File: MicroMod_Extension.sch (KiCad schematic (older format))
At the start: 1 part, among them J1 2199230-4

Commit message: inductor type
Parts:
- added C1, C2, C3, C5: 100n, Capacitor_SMD:C_0402_1005Metric, symbol Device:C
- added C4: 47n, Capacitor_SMD:C_0402_1005Metric, symbol Device:C
- added C?: 1u, Capacitor_SMD:C_0402_1005Metric, symbol Device:C
- added C?: 220p, Capacitor_SMD:C_0402_1005Metric, symbol Device:C
- added J2: XKB_U262-16XN-4BVC11, Connector_USB:USB_C_Receptacle_XKB_U262-16XN-4BVC11, symbol MicroMod_Extension:XKB_U262-16XN-4BVC11
- added L?: 2nH, symbol Device:L
- added U1: 24aa64ft-eot, Package_TO_SOT_SMD:SOT-23-5, symbol MicroMod_Extension:24aa64ft-eot
- added U2: nRF51822-QFAA-R7, Package_DFN_QFN:QFN-48-1EP_6x6mm_P0.4mm_EP4.6x4.6mm, symbol MCU_Nordic:nRF51x22-QFxx
- added U?: RFX2411N, symbol MicroMod_Extension:RFX2411N
- added Y1: TSX-3225_16.0000MF18X-AC3, XTAL_TSX-3225_16.0000MF18X-AC3, symbol MicroMod_Extension:TSX-3225_16.0000MF18X-AC3
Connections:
- net E_SCL: now also U1.1 (SCL)
- net E_SDA: now also U1.3 (SDA)
- net GND: now also C2.2, C3.2, C4.1, C5.1, C?.2, C?.2, J2.A1 (GND), J2.A12 (GND), J2.B1 (GND), J2.B12 (GND), J2.S1 (SHELD), U1.2 (VSS), U1.5 (WP), U2.13 (VSS), U2.33 (VSS), U2.34 (VSS), U2.49 (EP), U?.1 (GND), U?.11 (GND), U?.13 (GND), U?.19 (GND), U?.21 (GND), Y1.2 (GND), Y1.4 (GND)
- net OTG_FS_D+: now also J2.A7 (D-), J2.B7 (D-)
- net OTG_FS_D-: now also J2.A6 (D+), J2.B6 (D+)
- net VBAT: now also U2.1 (VDD), U2.12 (VDD), U2.35 (AVDD), U2.36 (AVDD)
- net VCC: now also U1.4 (VCC)
- new net: C4.2, U2.29 (DEC2)
- new net: C2.1, U2.37 (XC1), Y1.1
- new net: C3.1, U2.38 (XC2), Y1.3 (2)
- new net: C5.2, U2.39 (DEC1)
- new net: C?.1, C?.1, U?.18 (VDD), U?.20 (VDD)
- new net NRF_SWCLK: U2.24 (SWDCLK)
- new net NRF_SWIO: U2.23 (SWDIO/~RST)
- new net VBUS: J2.A4 (VBUS), J2.A9 (VBUS), J2.B4 (VBUS), J2.B9 (VBUS)
- no-connect marks 0 -> 19

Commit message: update RF
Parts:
- removed C?: 1u, Capacitor_SMD:C_0402_1005Metric, symbol Device:C
- removed C?: 220p, Capacitor_SMD:C_0402_1005Metric, symbol Device:C
- removed L?: 2nH, symbol Device:L
- removed U?: RFX2411N, symbol MicroMod_Extension:RFX2411N
- added C? (x2): 220p, Capacitor_SMD:C_0402_1005Metric, symbol Device:C
- added C?: 4.7u, Capacitor_SMD:C_0402_1005Metric, symbol Device:C
- added C?: 2.2n, Capacitor_SMD:C_0402_1005Metric, symbol Device:C
- added C?: 2.5p, Capacitor_SMD:C_0402_1005Metric, symbol Device:C
- added E?: 2450AT18B100E, MicroMod_Extension:XDCR_2450AT18B100E, symbol MicroMod_Extension:2450AT18B100E
- added FL1: 2450BM14E0003T, FIL_2450BM14E0003T, symbol MicroMod_Extension:2450BM14E0003T
- added FL? (x2): ADFC15-2450.00-A-T, MicroMod_Extension:FIL_ADFC15-2450.00-A-T, symbol MicroMod_Extension:ADFC15-2450.00-A-T
- added J?: RSP-122811-01, MicroMod_Extension:SAMTEC_RSP-122811-01, symbol MicroMod_Extension:RSP-122811-01
- added L? (x2): 2nH, Inductor_SMD:L_0402_1005Metric, symbol Device:L
- added L?: 1nH, Inductor_SMD:L_0402_1005Metric, symbol Device:L
- added L?: 4.7nH, Inductor_SMD:L_0402_1005Metric, symbol Device:L
- added R? (x2): 10K, Resistor_SMD:R_0402_1005Metric, symbol Device:R
- added U?: RFX2411N, symbol MicroMod_Extension:RFX2411N
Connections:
- net GND: now also C?.1, C?.1, C?.1, C?.1, FL1.2 (GND), FL1.6 (GND), FL?.1 (GND), FL?.1 (GND), FL?.3 (GND), FL?.3 (GND), J?.G1, J?.G2, L?.2, L?.2, U?.1 (GND), U?.11 (GND), U?.13 (GND), U?.19 (GND), U?.2 (NC), U?.21 (GND), U?.4 (NC)
- net at U2.30 (VDD_PA): now also C?.2, FL1.5 (DC_FEED), R?.1
- net at U2.31 (ANT1): now also FL1.3 (BALANCED_PORT1)
- net at U2.32 (ANT2): now also FL1.4 (BALANCED_PORT2)
- new net: FL1.1 (UNBALANCED_PORT), U?.5 (TXRX)
- new net: FL?.2 (OUT/IN), J?.1
- new net: FL?.4 (IN/OUT), U?.12 (ANT_B)
- new net: FL?.4 (IN/OUT), U?.14 (ANT_A)
- new net: L?.1, U?.15 (IND)
- new net: C?.2, C?.2, C?.2, U?.18 (VDD), U?.20 (VDD)
- new net: R?.2, U?.6 (TXEN)
- new net: C?.2, FL?.2 (OUT/IN)
- new net: C?.1, L?.1, L?.2
- new net: E?.1, L?.1
- new net PA_MODE: U?.9 (MODE)
- new net PA_RXEN: U?.7 (RXEN)
- new net PA_SW_ANT: U?.10 (SW_ANT)
- no-connect marks 19 -> 18
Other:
- note added: "4-layer, single ended, JLC7628: 11.55mil track width on outer layer"
- note added: "This balun matches ANT1 and ANT2 to 50 ohm."
- note added: "this line should have 50ohm inpedence matching"
- moved on the sheet: C2, C3, C4, C5, U2, Y1

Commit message: add power management
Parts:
- added C10, C19, C20, C21, C22: 1u, Capacitor_SMD:C_0402_1005Metric, symbol Device:C
- added C12: 10u, Capacitor_SMD:C_0402_1005Metric, symbol Device:C
- added C13, C9: 10n, Capacitor_SMD:C_0402_1005Metric, symbol Device:C
- added C18: 22u, Capacitor_SMD:C_0402_1005Metric, symbol Device:C
- added C6, C7, C8: 100n, Capacitor_SMD:C_0402_1005Metric, symbol Device:C
- added D1: LED, MicroMod_Extension:LED-0603, symbol Device:LED
- added D2, D4: 150066RG74000, MicroMod_Extension:150066RG74000, symbol MicroMod_Extension:150066RG74000
- added D3: SMF4L17A, Diode_SMD:D_SOD-123, symbol Device:D_TVS
- added D5: MBR0520-TP, Diode_SMD:D_SOD-123, symbol Device:D
- added L5: 2.2uH-TYA2520102R2M-10, Inductor_SMD:L_1008_2520Metric, symbol Device:L
- added R1, R10, R5, R8, R9: 150r, Resistor_SMD:R_0402_1005Metric, symbol Device:R
- added R11: 510k, Resistor_SMD:R_0402_1005Metric, symbol Device:R
- added R12: 110k, Resistor_SMD:R_0402_1005Metric, symbol Device:R
- added R14: 430K, Resistor_SMD:R_0402_1005Metric, symbol Device:R
- added R15: 82K, Resistor_SMD:R_0402_1005Metric, symbol Device:R
- added R2, R3: 5.1k, Resistor_SMD:R_0402_1005Metric, symbol Device:R
- added R6, R7: 10K, Resistor_SMD:R_0402_1005Metric, symbol Device:R
- added SW1: TL1014BF160QG, MicroMod_Extension:E-Switch-TL1014BF160QG-0, symbol MicroMod_Extension:TL1014BF160QG
- added TP1, TP2, TP3: TestPoint, TestPoint:TestPoint_Pad_D1.0mm, symbol Connector:TestPoint
- added U4: TPS62170DSG, Package_SON:WSON-8-1EP_2x2mm_P0.5mm_EP0.9x1.6mm_ThermalVias, symbol Regulator_Switching:TPS62170DSG
- added U5, U6: NCP702SN30T1G, Package_TO_SOT_SMD:TSOT-23-5, symbol MicroMod_Extension:NCP702SN30T1G
- C2, C3: value 100n -> 12p
- U3: renamed from U?; footprint (none) -> Package_DFN_QFN:QFN-20-1EP_3x3mm_P0.4mm_EP1.65x1.65mm
- gave numbers to parts that had none: 15
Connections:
- net BOOT0 is gone; now on net STM_BOOT0: J1.70
- net NRST is gone; now on net STM_NRST: J1.67
- net OTG_FS_VBUS is gone; now on net VBUS: J1.9
- net GND: now also C10.2, C12.2, C13.2, C18.1, C19.1, C20.1, C21.2, C22.2, C6.2, C7.2, C8.2, C9.2, D1.1 (K), D3.2 (A2), R12.2, R15.1, R2.2, R3.2, R7.2, SW1.2, SW1.4, U4.1 (PGND), U4.4 (AGND), U4.9 (PAD), U5.2 (GND), U6.2 (GND)
- net GREEN_L: now also R8.1
- net GREEN_R: now also R10.1
- net NRF_CTRL: now also U2.20 (P0.14)
- net NRF_RX: now also U2.3 (P0.30)
- net NRF_TX: now also U2.48 (P0.29)
- net PA_MODE: now also U2.27 (P0.19)
- net PA_RXEN: now also U2.28 (P0.20)
- net PA_SW_ANT: now also U2.26 (P0.18)
- net RED_L: now also R5.1
- net RED_R: now also R9.1
- net VBAT: now also U2.5 (P0.1), C13.1, R11.2, R12.1; no longer J1.73, U2.1 (VDD), U2.12 (VDD), U2.35 (AVDD), U2.36 (AVDD)
- net VBUS: now also D5.2 (A), R6.1
- net VCC: now also C21.1, D2.3, D2.4, D4.3, D4.4, TP2.1, U6.5 (OUT)
- net VEN_D: now reaches U2.16 (P0.10)
- net VEN_D: now also R6.2, R7.1, U6.3 (EN)
- net LED_BLUE: now reaches U2.19 (P0.13)
- net LED_BLUE: now also R1.1
- net SWITCH: now reaches U2.25 (P0.17)
- net SWITCH: now also SW1.1, SW1.3
- net STM_NRST: now reaches U2.40 (P0.21)
- net STM_BOOT0: now reaches U2.41 (P0.22)
- net PM_PGOOD: now reaches U2.8 (P0.4)
- net PM_PGOOD: now also U4.8 (PG)
- net VCC_NRF: now reaches C14.2, C15.2, C16.2, U3.18 (VDD), U3.20 (VDD)
- net VCC_NRF: now also J1.73, U2.1 (VDD), U2.12 (VDD), U2.35 (AVDD), U2.36 (AVDD), C10.1, C22.1, C6.1, C7.1, C8.1, C9.1, TP3.1, U5.5 (OUT)
- net at J2.A5 (CC1): now also R2.1
- net at J2.B5 (CC2): now also R3.1
- net E_SPI_CLK renamed E_SPI_SCK
- net SPI2_CLK renamed SPI2_SCK
- new net: R14.1, R15.2, U4.5 (FB)
- new net: C18.2, C19.2, C20.2, D5.1 (K), L5.1, R14.2, TP1.1, U4.6 (VOS), U5.1 (IN), U5.3 (EN), U6.1 (IN)
- new net: L5.2, U4.7 (SW)
- new net: D1.2 (A), R1.2
- new net: D2.1, R5.2
- new net: D2.2, R8.2
- new net: D4.1, R9.2
- new net: D4.2, R10.2
- new net BATT: C12.1, D3.1 (A1), R11.1, U4.2 (VIN), U4.3 (EN)
- no-connect marks 18 -> 33
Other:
- note added: "4-layer, single ended, JLC7628: 11.55mil track width on outer layer for 50 ohm."
- note added: "EEPROM"
- note added: "USB-C"
- note removed: "4-layer, single ended, JLC7628: 11.55mil track width on outer layer"
- note removed: "this line should have 50ohm inpedence matching"
- moved on the sheet: U1

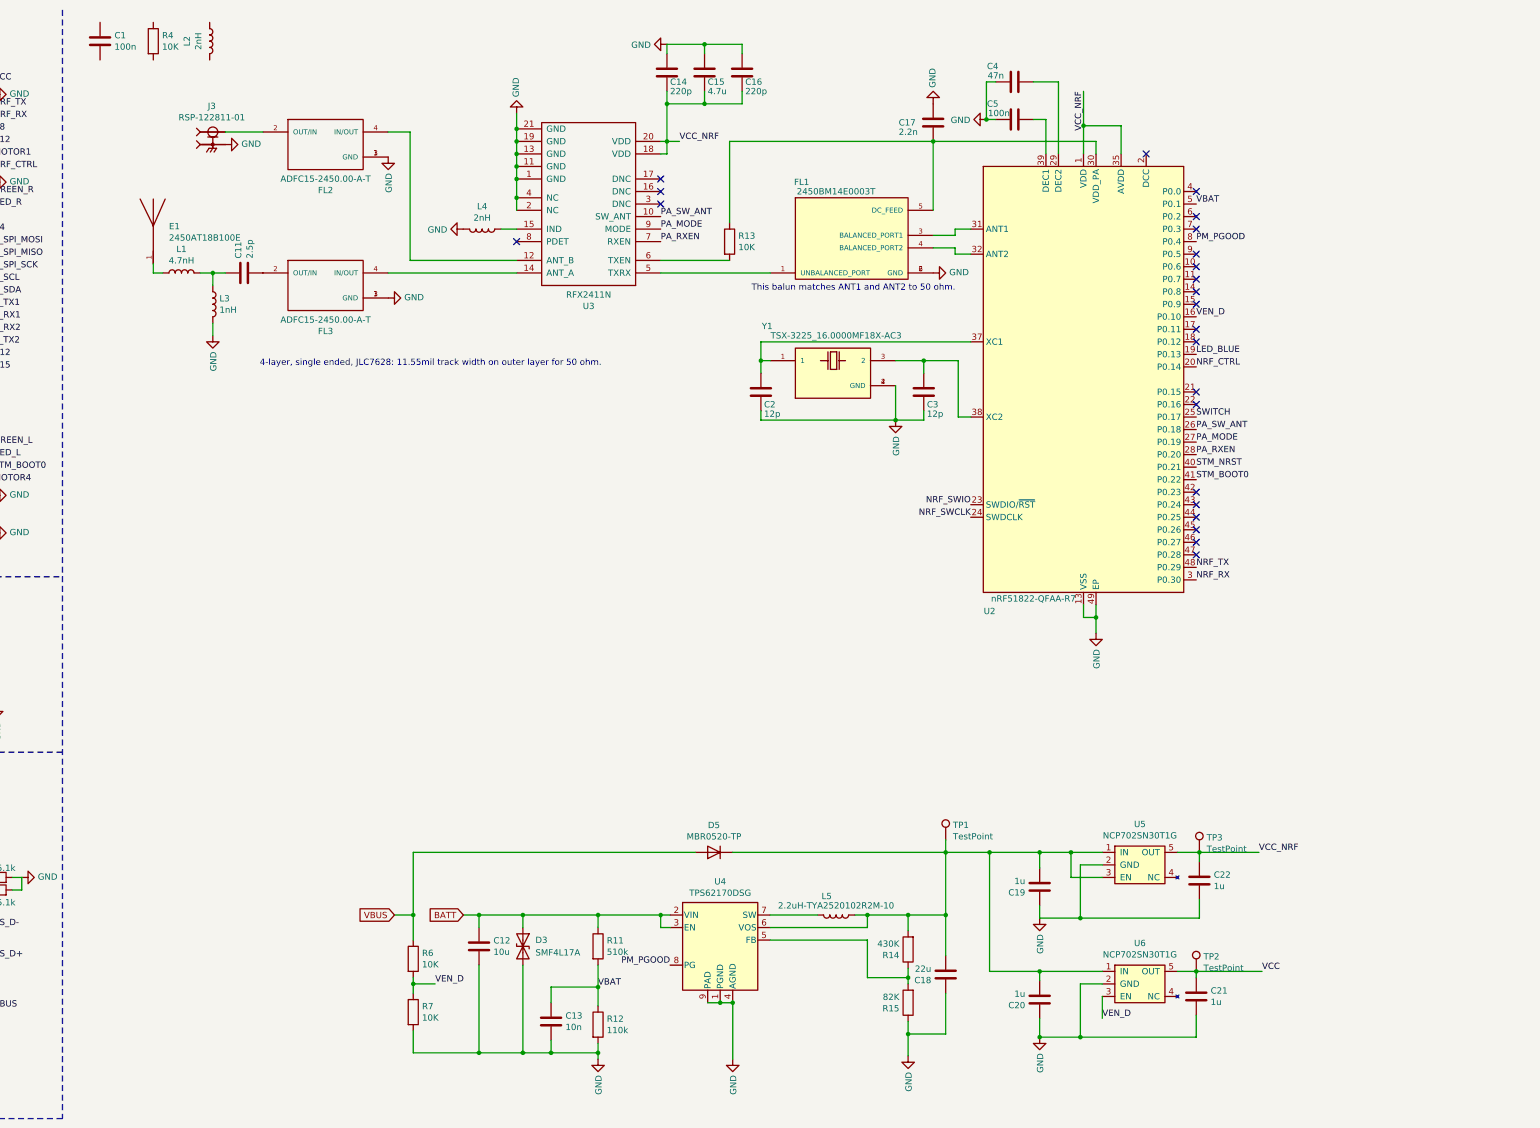
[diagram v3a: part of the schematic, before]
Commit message: add bmi270 and bmp384
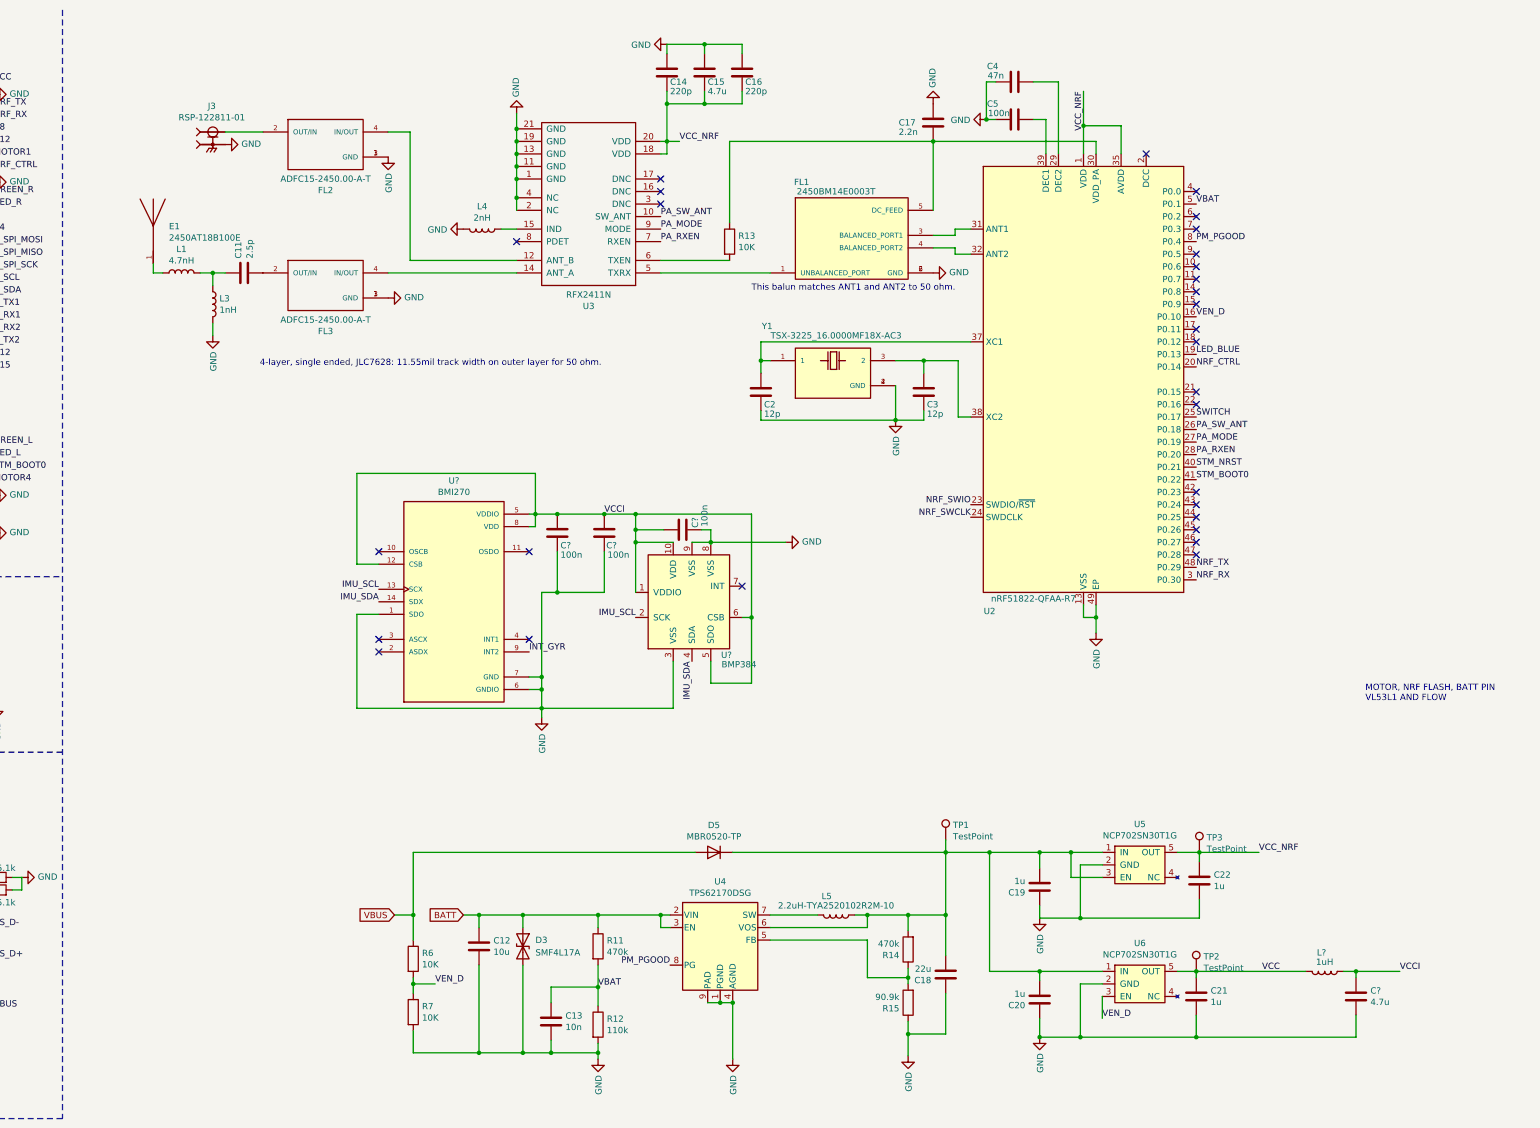
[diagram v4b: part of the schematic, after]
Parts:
- removed C1: 100n, Capacitor_SMD:C_0402_1005Metric, symbol Device:C
- removed L2: 2nH, Inductor_SMD:L_0402_1005Metric, symbol Device:L
- removed R4: 10K, Resistor_SMD:R_0402_1005Metric, symbol Device:R
- added C? (x3): 100n, Capacitor_SMD:C_0402_1005Metric, symbol Device:C
- added C?: 4.7u, Capacitor_SMD:C_0402_1005Metric, symbol Device:C
- added L?: 1uH, Inductor_SMD:L_0402_1005Metric, symbol Device:L
- added U?: BMI270, XDCR_BMI270, symbol MicroMod_Extension:BMI270
- added U?: BMP384, symbol MicroMod_Extension:BMP384
- C18: footprint Capacitor_SMD:C_0402_1005Metric -> Capacitor_SMD:C_0805_2012Metric
- R11: value 510k -> 470k
- R14: value 430K -> 470k
- R15: value 82K -> 90.9k
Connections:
- net GND: now also C?.1, C?.1, C?.2, C?.2, U?.1 (SDO), U?.3 (VSS), U?.6 (GNDIO), U?.7 (GND), U?.8 (VSS), U?.9 (VSS)
- net IMU_SCL: now also U?.13 (SCX), U?.2 (SCK)
- net IMU_SDA: now also U?.14 (SDX), U?.4 (SDA)
- net INT_GYR: now also U?.9 (INT2)
- net VCC: now also L?.2
- new net VCCI: C?.1, C?.1, C?.2, C?.2, L?.1, U?.1 (VDDIO), U?.10 (VDD), U?.12 (CSB), U?.5 (SDO), U?.5 (VDDIO), U?.6 (CSB), U?.8 (VDD)
- no-connect marks 33 -> 39
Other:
- note added: "MOTOR, NRF FLASH, BATT PIN\nVL53L1 AND FLOW"
